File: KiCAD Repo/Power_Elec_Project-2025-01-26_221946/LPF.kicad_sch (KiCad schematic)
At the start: 2 parts, among them U1 LM358

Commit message: LPF design
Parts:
- added C1: 0.1uF, symbol Device:C
- added C2, C3: C, symbol Device:C
- added L1: L, symbol Device:L
- added R2: 172k, Resistor_SMD:R_0603_1608Metric, symbol Device:R
- added R3: 10K, Resistor_SMD:R_0805_2012Metric, symbol Device:R
- R1: value 10k -> 10K
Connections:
- net +3.3V: now also U1.8 (V+), C1.1
- net GND: now also R1.2, U1.4 (V-), C1.2, C2.2, C3.2, R3.2
- net INPUT: now also R2.2
- net OUTPUT: now also U1.1, U1.2 (-)
- net at U1.3 (+): now also C3.1, L1.2, R3.1; no longer R1.1
- new net: C2.1, L1.1, R1.1, R2.1
- no-connect marks 0 -> 3
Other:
- note added: "Exoecting a Quiescent output of 30V. The output of the opamp is between 0v to 3.3v Therefore R1 and R2 should generate the gain to scale 30v down to 3.3v/2 = 1.65v If R1 = 10k, R2~= 172k"
- moved on the sheet: R1, U1A, U1B, U1C

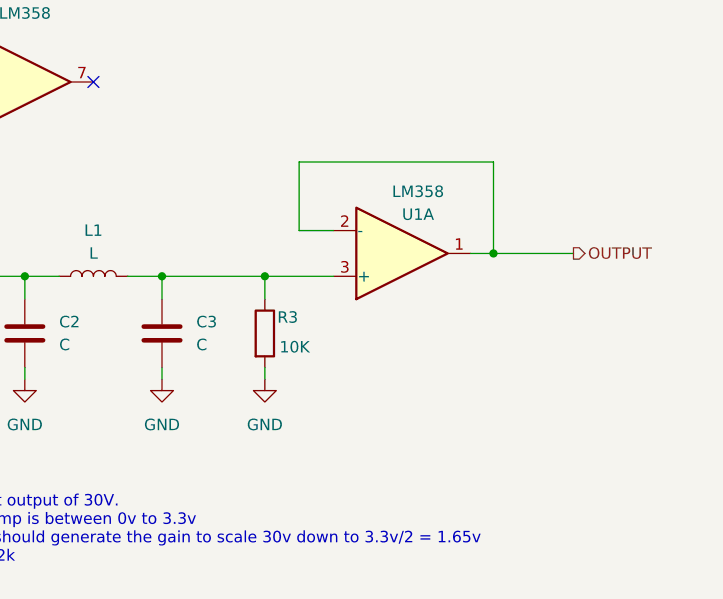
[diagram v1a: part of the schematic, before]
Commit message: Pi LPF simulation
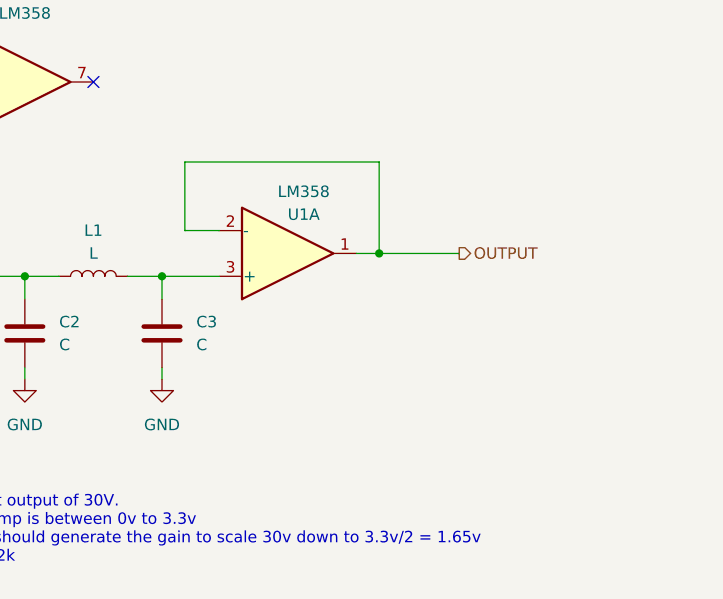
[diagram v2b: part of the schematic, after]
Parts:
- removed R3: 10K, Resistor_SMD:R_0805_2012Metric, symbol Device:R
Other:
- moved on the sheet: U1A
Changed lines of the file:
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@@
-	)
-	(junction
-		(at 148.59 83.82)
-		(diameter 0)
-		(color 0 0 0 0)
 	)
 	(junction
@@
 	)
 	(junction
-		(at 173.99 81.28)
+		(at 161.29 81.28)
 		(diameter 0)
 		(color 0 0 0 0)
@@
 	(wire
 		(pts
-			(xy 152.4 78.74) (xy 152.4 71.12)
-		)
-		(stroke
-			(width 0)
-			(type default)
-		)
-	)
-	(wire
-		(pts
-			(xy 148.59 83.82) (xy 148.59 86.36)
+			(xy 139.7 78.74) (xy 139.7 71.12)
 		)
 		(stroke
@@
 	(wire
 		(pts
-			(xy 148.59 83.82) (xy 156.21 83.82)
-		)
-		(stroke
-			(width 0)
-			(type default)
-		)
-	)
-	(wire
-		(pts
-			(xy 148.59 95.25) (xy 148.59 93.98)
-		)
-		(stroke
-			(width 0)
-			(type default)
-		)
-	)
-	(wire
-		(pts
 			(xy 85.09 101.6) (xy 85.09 104.14)
 		)
@@
 	(wire
 		(pts
-			(xy 173.99 81.28) (xy 171.45 81.28)
+			(xy 161.29 81.28) (xy 158.75 81.28)
 		)
 		(stroke
@@
 	(wire
 		(pts
-			(xy 156.21 78.74) (xy 152.4 78.74)
+			(xy 143.51 78.74) (xy 139.7 78.74)
 		)
 		(stroke
@@
 	(wire
 		(pts
-			(xy 173.99 81.28) (xy 182.88 81.28)
+			(xy 161.29 81.28) (xy 170.18 81.28)
 		)
 		(stroke
@@
 	(wire
 		(pts
-			(xy 137.16 83.82) (xy 148.59 83.82)
-		)
-		(stroke
-			(width 0)
-			(type default)
-		)
-	)
-	(wire
-		(pts
-			(xy 152.4 71.12) (xy 173.99 71.12)
+			(xy 137.16 83.82) (xy 143.51 83.82)
+		)
+		(stroke
+			(width 0)
+			(type default)
+		)
+	)
+	(wire
+		(pts
+			(xy 139.7 71.12) (xy 161.29 71.12)
 		)
 		(stroke
@@
 	(wire
 		(pts
-			(xy 173.99 71.12) (xy 173.99 81.28)
+			(xy 161.29 71.12) (xy 161.29 81.28)
 		)
 		(stroke
@@
 	(hierarchical_label "OUTPUT"
 		(shape output)
-		(at 182.88 81.28 0)
+		(at 170.18 81.28 0)
 		(effects
 			(font
@@
 	)
 	(symbol
-		(lib_id "Device:R")
-		(at 148.59 90.17 0)
-		(unit 1)
-		(exclude_from_sim no)
-		(in_bom yes)
-		(on_board yes)
-		(dnp no)
-		(property "Reference" "R3"
-			(at 151.13 88.392 0)
-			(effects
-				(font
-					(size 1.27 1.27)
-				)
-			)
-		)
-		(property "Value" "10K"
-			(at 151.892 91.694 0)
-			(effects
-				(font
-					(size 1.27 1.27)
-				)
-			)
-		)
-		(property "Footprint" "Resistor_SMD:R_0805_2012Metric"
-			(at 146.812 90.17 90)
-			(effects
-				(font
-					(size 1.27 1.27)
-				)
-				(hide yes)
-			)
-		)
-		(property "Datasheet" "~"
-			(at 148.59 90.17 0)
-			(effects
-				(font
-					(size 1.27 1.27)
-				)
-				(hide yes)
-			)
-		)
-		(property "Description" "Resistor"
-			(at 148.59 90.17 0)
-			(effects
-				(font
-					(size 1.27 1.27)
-				)
-				(hide yes)
-			)
-		)
-		(property "Part Number" ""
-			(at 148.59 90.17 90)
-			(effects
-				(font
-					(size 1.27 1.27)
-				)
-				(hide yes)
-			)
-		)
-		(pin "1"
-		)
-		(pin "2"
-		)
-		(instances
-			(project "Power_Elec_Project"
-				(path "/ecd51ed2-b30f-41c1-93fa-3d04786e684e/24945a6e-9cf1-4d51-984e-568b86374556"
-					(reference "R3")
-					(unit 1)
-				)
-			)
-		)
-	)
-	(symbol
 		(lib_id "power:GND")
 		(at 85.09 87.63 0)
@@
 	)
 	(symbol
-		(lib_id "power:GND")
-		(at 148.59 95.25 0)
-		(unit 1)
-		(exclude_from_sim no)
-		(in_bom yes)
-		(on_board yes)
-		(dnp no)
-		(fields_autoplaced yes)
-		(property "Reference" "#PWR16"
-			(at 148.59 101.6 0)
-			(effects
-				(font
-					(size 1.27 1.27)
-				)
-				(hide yes)
-			)
-		)
-		(property "Value" "GND"
-			(at 148.59 100.33 0)
-			(effects
-				(font
-					(size 1.27 1.27)
-				)
-			)
-		)
-		(property "Footprint" ""
-			(at 148.59 95.25 0)
-			(effects
-				(font
-					(size 1.27 1.27)
-				)
-				(hide yes)
-			)
-		)
-		(property "Datasheet" ""
-			(at 148.59 95.25 0)
-			(effects
-				(font
-					(size 1.27 1.27)
-				)
-				(hide yes)
-			)
-		)
-		(property "Description" "Power symbol creates a global label with name \"GND\" , ground"
-			(at 148.59 95.25 0)
-			(effects
-				(font
-					(size 1.27 1.27)
-				)
-				(hide yes)
-			)
-		)
-		(pin "1"
-		)
-		(instances
-			(project "Power_Elec_Project"
-				(path "/ecd51ed2-b30f-41c1-93fa-3d04786e684e/24945a6e-9cf1-4d51-984e-568b86374556"
-					(reference "#PWR16")
-					(unit 1)
-				)
-			)
-		)
-	)
-	(symbol
 		(lib_id "power:+3.3V")
 		(at 85.09 101.6 0)
@@
 	(symbol
 		(lib_id "Amplifier_Operational:LM358")
-		(at 163.83 81.28 0)
+		(at 151.13 81.28 0)
 		(mirror x)
 		(unit 1)
@@
 		(dnp no)
 		(property "Reference" "U1"
-			(at 165.608 76.962 0)
+			(at 152.908 76.962 0)
 			(effects
 				(font
@@
 		)
 		(property "Value" "LM358"
-			(at 165.608 74.422 0)
+			(at 152.908 74.422 0)
 			(effects
 				(font
@@
 		)
 		(property "Footprint" "Package_SO:VSSOP-8_3x3mm_P0.65mm"
-			(at 163.83 81.28 0)
+			(at 151.13 81.28 0)
 			(effects
 				(font
@@
 		)
 		(property "Datasheet" "www.ti.com/lit/ds/symlink/lm358.pdf?HQS=dis-dk-null-digikeymode-dsf-pf-null-wwe&ts=1739934979714&ref_url=https%253A%252F%252Fwww.ti.com%252Fgeneral%252Fdocs%252Fsuppproductinfo.tsp%253FdistId%253D10%2526gotoUrl%253Dhttps%253A%252F%252Fwww.ti.com%252Flit%252Fgpn%252Flm358"
-			(at 163.83 81.28 0)
+			(at 151.13 81.28 0)
 			(effects
 				(font
@@
 		)
 		(property "Description" "Low-Power, Dual Operational Amplifiers, DIP-8/SOIC-8/TO-99-8"
-			(at 163.83 81.28 0)
+			(at 151.13 81.28 0)
 			(effects
 				(font
@@
 		)
 		(property "Part Number" "LM358DGKR"
-			(at 163.83 81.28 0)
-			(effects
-				(font
+			(at 151.13 81.28 0)
+			(effects
+				(font
